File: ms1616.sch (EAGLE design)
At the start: 90 parts, among them IC101 ATMEGA32-PU, IC102 MAX483CPA, IC103 74594N, IC104 74594N, IC201 LTV847, IC202 LTV847, IC203 LTV847, IC204 LTV847, K301 S202S02, K302 S202S02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

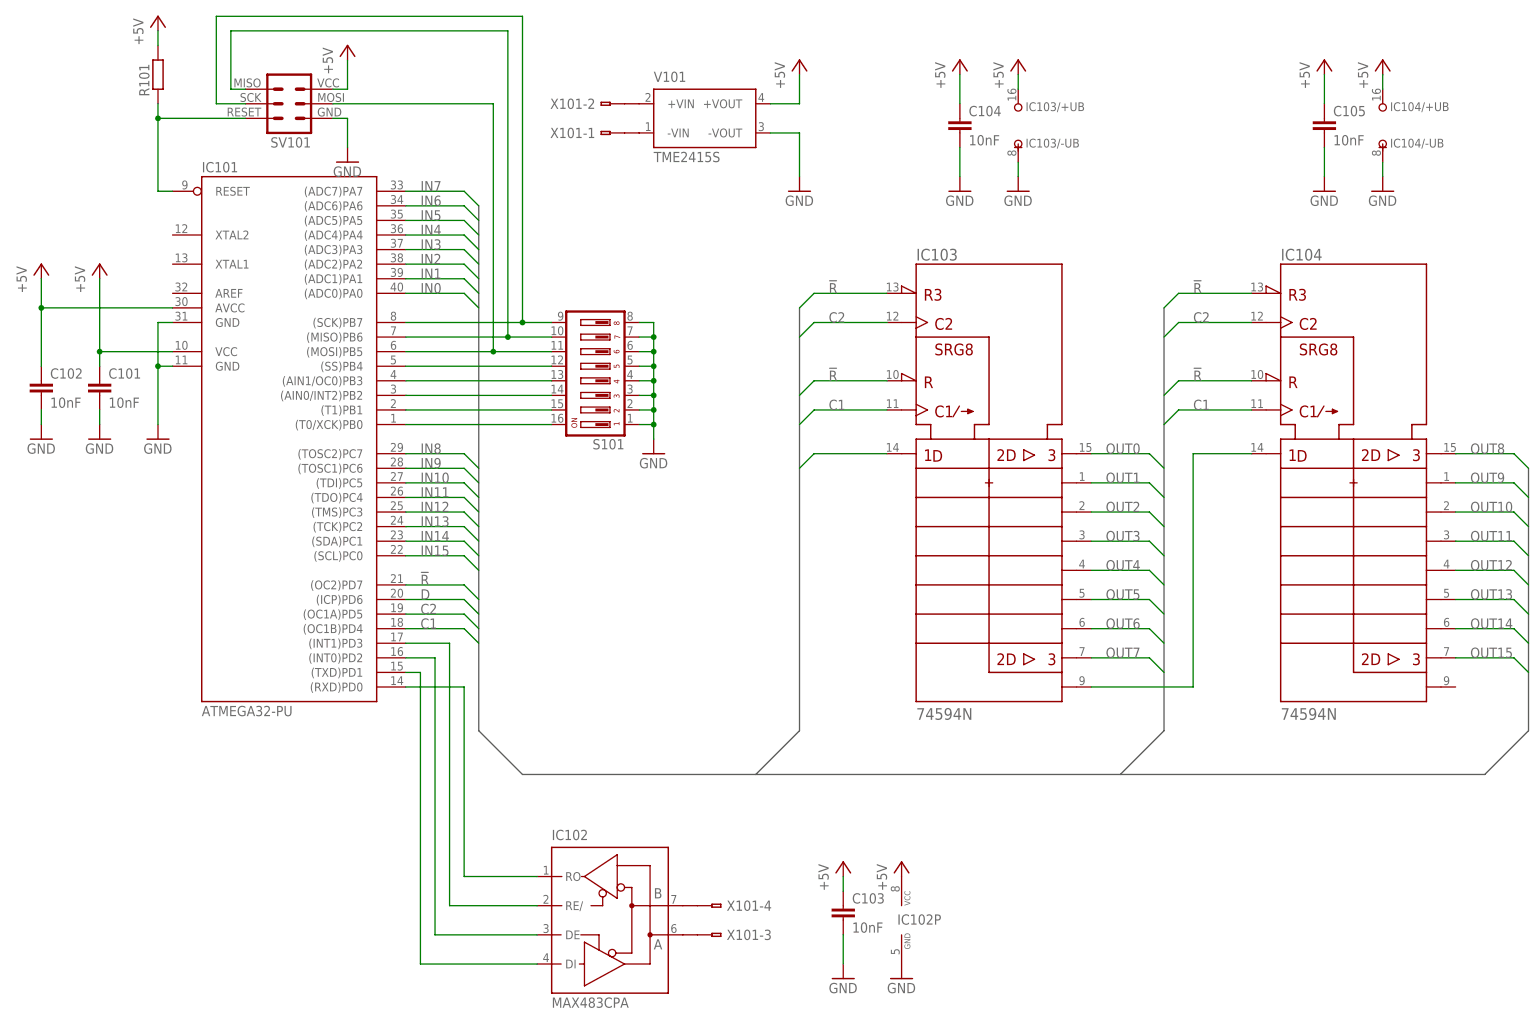
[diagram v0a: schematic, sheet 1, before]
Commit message: 74594 durch 74HC594 ersetzt
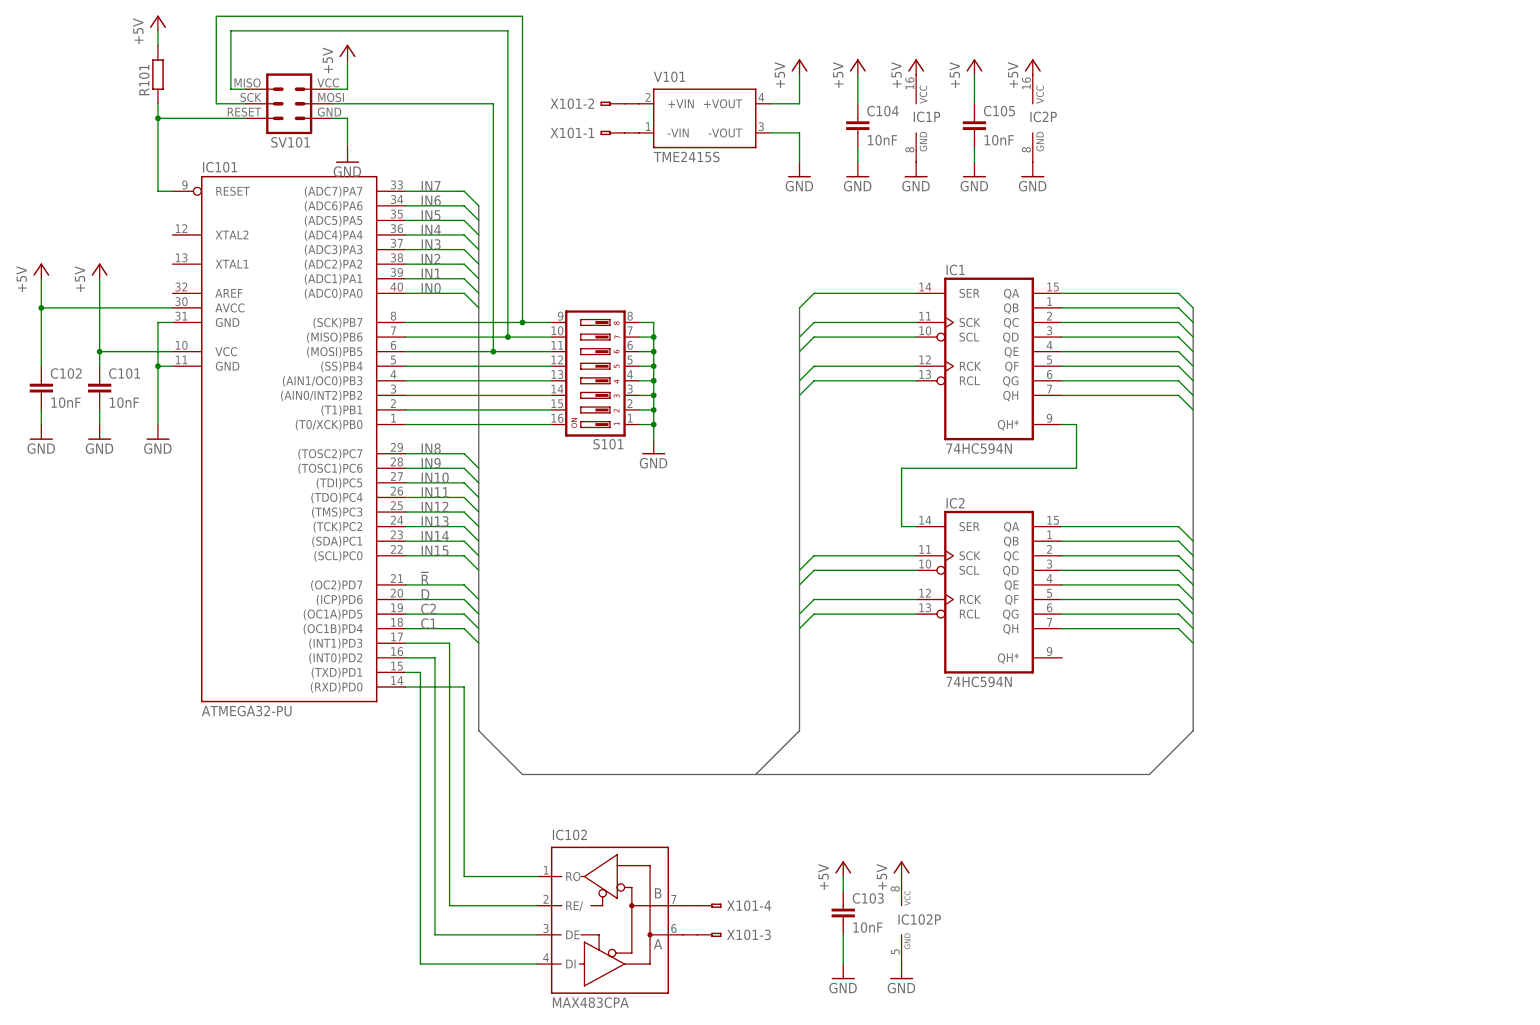
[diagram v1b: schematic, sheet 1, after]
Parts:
- removed IC103, IC104: 74594N, 74ttl-din:74594N
- added IC1, IC2: 74HC594N, 74xx-eu:74HC594N
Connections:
- net !R: now also IC1A.RCL, IC1A.SCL, IC2A.RCL, IC2A.SCL; no longer IC1031.!RCLR, IC1031.!SRCLR, IC1041.!RCLR, IC1041.!SRCLR
- net +5V: now also IC1P.VCC, IC2P.VCC; no longer IC103/+UB.+UB, IC104/+UB.+UB
- net C1: now also IC1A.SCK, IC2A.SCK; no longer IC1031.SRCK, IC1041.SRCK
- net C2: now also IC1A.RCK, IC2A.RCK; no longer IC1031.RCK, IC1041.RCK
- net D: now also IC1A.SER; no longer IC1031.SER
- net GND: now also IC1P.GND, IC2P.GND; no longer IC103/-UB.-UB, IC104/-UB.-UB
- net N$58: now also IC1A.QH*, IC2A.SER; no longer IC1031.QH*, IC1041.SER
- net OUT0: now also IC1A.QA; no longer IC1031.QA
- net OUT1: now also IC1A.QB; no longer IC1031.QB
- net OUT10: now also IC2A.QC; no longer IC1041.QC
- net OUT11: now also IC2A.QD; no longer IC1041.QD
- net OUT12: now also IC2A.QE; no longer IC1041.QE
- net OUT13: now also IC2A.QF; no longer IC1041.QF
- net OUT14: now also IC2A.QG; no longer IC1041.QG
- net OUT15: now also IC2A.QH; no longer IC1041.QH
- net OUT2: now also IC1A.QC; no longer IC1031.QC
- net OUT3: now also IC1A.QD; no longer IC1031.QD
- net OUT4: now also IC1A.QE; no longer IC1031.QE
- net OUT5: now also IC1A.QF; no longer IC1031.QF
- net OUT6: now also IC1A.QG; no longer IC1031.QG
- net OUT7: now also IC1A.QH; no longer IC1031.QH
- net OUT8: now also IC2A.QA; no longer IC1041.QA
- net OUT9: now also IC2A.QB; no longer IC1041.QB
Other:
- moved on the sheet: C104, C105

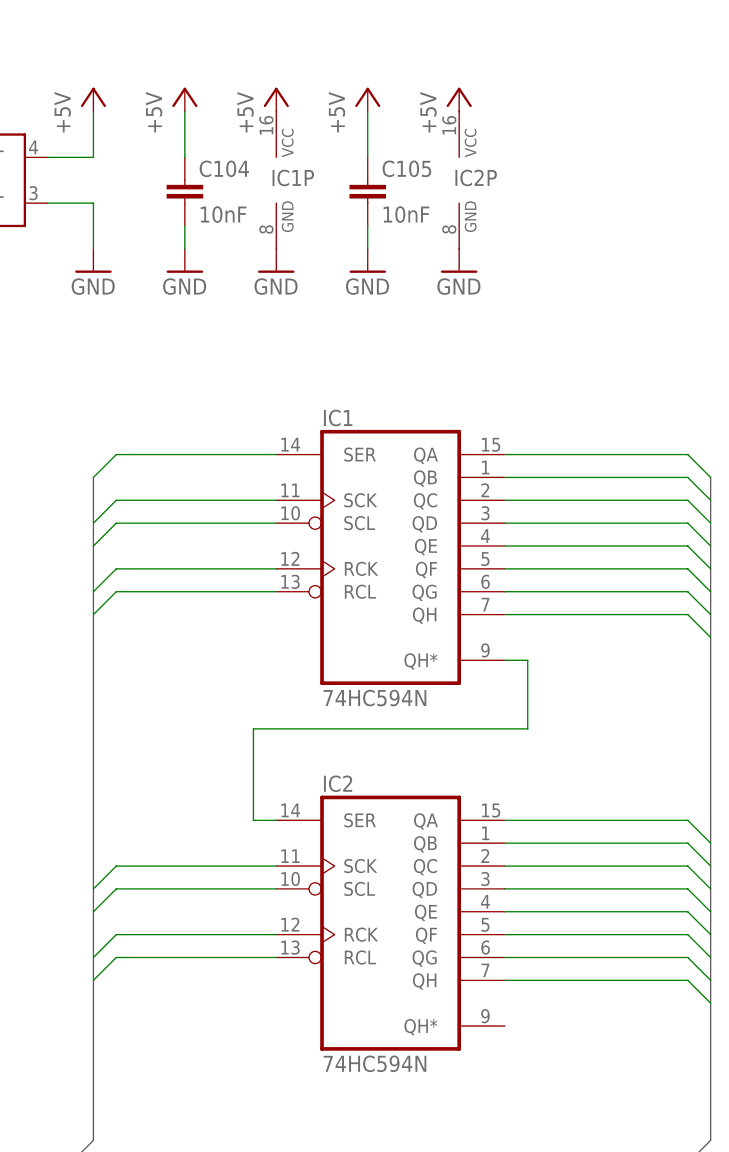
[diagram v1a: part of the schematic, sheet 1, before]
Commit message: Leichte korrekturen an Schematik und Layout
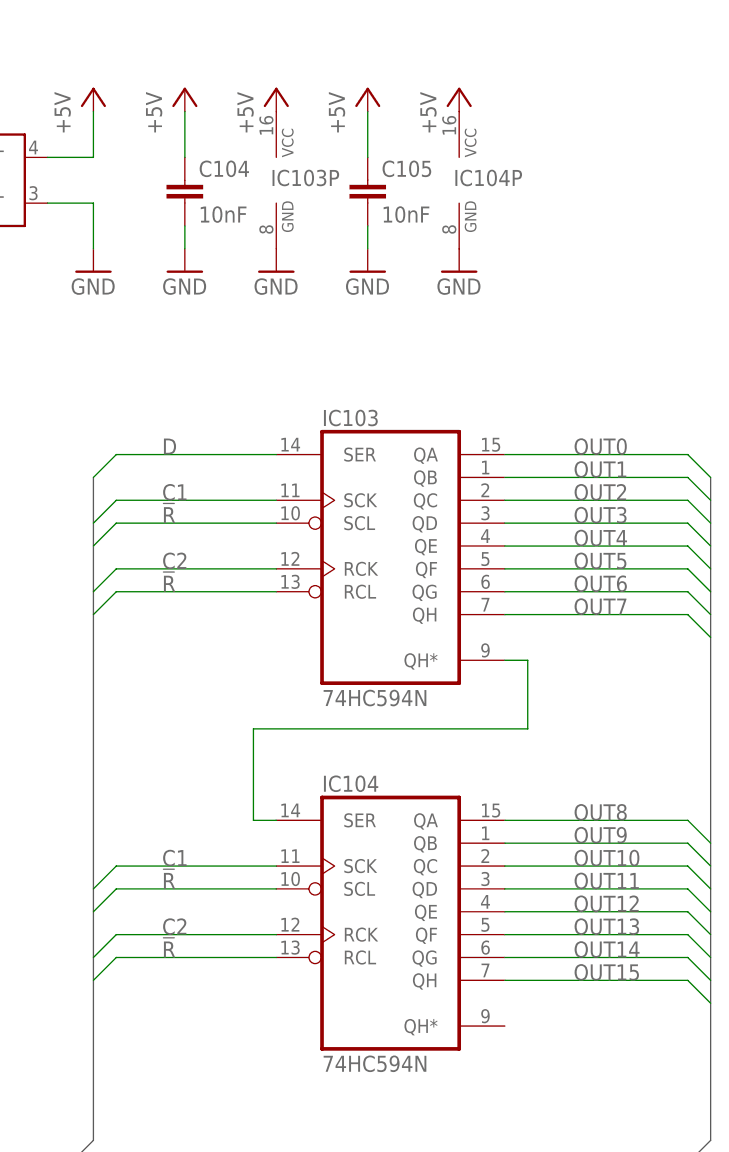
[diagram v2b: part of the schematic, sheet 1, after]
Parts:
- renumbered IC1 to IC103, IC2 to IC104

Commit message: Echtzeituhr eingebaut
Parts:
- added C1: 10nF, passiv:C_025-025X050
- added IC105: 74HC594N, 74xx-eu:74HC594N
- added Q1: (no value), passiv:Q_HC49S
- IC102: value MAX483CPA -> DS1337; device ic-wandler:MAX483CPA -> ic-controller:DS1337
- IC103: value 74HC594N -> MAX483CPA; device 74xx-eu:74HC594N -> ic-wandler:MAX483CPA
- S101: device schalter:DIP08YL -> schalter:DIP04YL
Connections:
- removed net N$128: IC101.(AIN0/INT2)PB2, S101.14
- removed net N$129: IC101.(AIN1/OC0)PB3, S101.13
- new net SCL: IC101.(T0/XCK)PB0, IC102G$1.SCL
- new net SDA: IC101.(T1)PB1, IC102G$1.SDA
- net !R: now also IC105A.RCL, IC105A.SCL; no longer IC103A.RCL, IC103A.SCL
- net +5V: now also C1.1, IC105P.VCC
- net C1: now also IC105A.SCK; no longer IC103A.SCK
- net C2: now also IC105A.RCK; no longer IC103A.RCK
- net D: now also IC104A.SER; no longer IC103A.SER
- net GND: now also C1.2, IC105P.GND; no longer S101.1, S101.2, S101.3, S101.4
- net N$122: now also S101.3; no longer S101.11
- net N$123: now also S101.2; no longer S101.10
- net N$124: now also IC103G$1.B; no longer IC102G$1.B
- net N$125: now also S101.1; no longer S101.9
- net N$126: now also IC102G$1.X1, Q1.2; no longer IC101.(T0/XCK)PB0, S101.16
- net N$127: now also IC102G$1.X2, Q1.1; no longer IC101.(T1)PB1, S101.15
- net N$130: now also S101.4; no longer S101.12
- net N$58: now also IC104A.QH*, IC105A.SER; no longer IC103A.QH*, IC104A.SER
- net N$61: now also IC103G$1.DI; no longer IC102G$1.DI
- net N$62: now also IC103G$1.RO; no longer IC102G$1.RO
- net N$63: now also IC103G$1.RE/; no longer IC102G$1.RE/
- net N$64: now also IC103G$1.DE; no longer IC102G$1.DE
- net N$74: now also IC103G$1.A; no longer IC102G$1.A
- net OUT0: now also IC104A.QA; no longer IC103A.QA
- net OUT1: now also IC104A.QB; no longer IC103A.QB
- net OUT10: now also IC105A.QC; no longer IC104A.QC
- net OUT11: now also IC105A.QD; no longer IC104A.QD
- net OUT12: now also IC105A.QE; no longer IC104A.QE
- net OUT13: now also IC105A.QF; no longer IC104A.QF
- net OUT14: now also IC105A.QG; no longer IC104A.QG
- net OUT15: now also IC105A.QH; no longer IC104A.QH
- net OUT2: now also IC104A.QC; no longer IC103A.QC
- net OUT3: now also IC104A.QD; no longer IC103A.QD
- net OUT4: now also IC104A.QE; no longer IC103A.QE
- net OUT5: now also IC104A.QF; no longer IC103A.QF
- net OUT6: now also IC104A.QG; no longer IC103A.QG
- net OUT7: now also IC104A.QH; no longer IC103A.QH
- net OUT8: now also IC105A.QA; no longer IC104A.QA
- net OUT9: now also IC105A.QB; no longer IC104A.QB
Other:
- moved on the sheet: IC102P, IC103P, IC104, IC104P, X101-3, X101-4

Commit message: Werte korrigiert
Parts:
- Q1: value (none) -> 32,768kHz
- R101: value (none) -> 10k
- V101: value TME2415S -> TME2405S; device schaltregler:TME2415S -> schaltregler:TME2405S; MPN (none) -> TME 2405S; OC_FARNELL (none) -> 1007547; OC_NEWARK (none) -> 51R5329
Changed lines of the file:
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@@
 <part name="GND25" library="versorgung" deviceset="GND" device=""/>
 <part name="P+2" library="versorgung" deviceset="+5V" device=""/>
-<part name="R101" library="passiv" deviceset="R_" device="0204/2V"/>
+<part name="R101" library="passiv" deviceset="R_" device="0204/2V" value="10k"/>
 <part name="P+1" library="versorgung" deviceset="+5V" device=""/>
 <part name="IC103" library="ic-wandler" deviceset="MAX48*" device="CPA" technology="3"/>
-<part name="V101" library="schaltregler" deviceset="TME?*" device="24" technology="15S"/>
+<part name="V101" library="schaltregler" deviceset="TME?*" device="24" technology="05S">
+<attribute name="MPN" value="TME 2405S"/>
+<attribute name="OC_FARNELL" value="1007547"/>
+<attribute name="OC_NEWARK" value="51R5329"/>
+</part>
 <part name="GND26" library="versorgung" deviceset="GND" device=""/>
 <part name="P+3" library="versorgung" deviceset="+5V" device=""/>
@@
 <part name="S101" library="schalter" deviceset="DIP04YL" device=""/>
 <part name="IC102" library="ic-controller" deviceset="DS1337" device=""/>
-<part name="Q1" library="passiv" deviceset="Q_" device="HC49S"/>
+<part name="Q1" library="passiv" deviceset="Q_" device="HC49S" value="32,768kHz"/>
 <part name="C1" library="passiv" deviceset="C_" device="025-025X050" value="10nF"/>
 <part name="P+12" library="versorgung" deviceset="+5V" device=""/>
@@
 <instance part="GND42" gate="1" x="182.88" y="5.08"/>
 <instance part="GND43" gate="1" x="172.72" y="5.08"/>
-<instance part="GND44" gate="1" x="139.7" y="96.52"/>
+<instance part="GND44" gate="1" x="139.7" y="106.68"/>
 <instance part="IC104" gate="A" x="198.12" y="114.3"/>
 <instance part="IC104" gate="P" x="185.42" y="154.94"/>
@@
 <segment>
 <pinref part="GND44" gate="1" pin="GND"/>
-<wire x1="137.16" y1="101.6" x2="139.7" y2="101.6" width="0.1524" layer="91"/>
-<wire x1="139.7" y1="101.6" x2="139.7" y2="99.06" width="0.1524" layer="91"/>
-<wire x1="137.16" y1="104.14" x2="139.7" y2="104.14" width="0.1524" layer="91"/>
-<wire x1="139.7" y1="104.14" x2="139.7" y2="101.6" width="0.1524" layer="91"/>
-<junction x="139.7" y="101.6"/>
-<wire x1="137.16" y1="106.68" x2="139.7" y2="106.68" width="0.1524" layer="91"/>
-<wire x1="139.7" y1="106.68" x2="139.7" y2="104.14" width="0.1524" layer="91"/>
-<junction x="139.7" y="104.14"/>
-<wire x1="137.16" y1="109.22" x2="139.7" y2="109.22" width="0.1524" layer="91"/>
-<wire x1="139.7" y1="109.22" x2="139.7" y2="106.68" width="0.1524" layer="91"/>
-<junction x="139.7" y="106.68"/>
 <wire x1="137.16" y1="111.76" x2="139.7" y2="111.76" width="0.1524" layer="91"/>
 <wire x1="139.7" y1="111.76" x2="139.7" y2="109.22" width="0.1524" layer="91"/>
-<junction x="139.7" y="109.22"/>
 <wire x1="137.16" y1="114.3" x2="139.7" y2="114.3" width="0.1524" layer="91"/>
 <wire x1="139.7" y1="114.3" x2="139.7" y2="111.76" width="0.1524" layer="91"/>
@@
 <segment>
 <pinref part="SV101" gate="1" pin="MISO"/>
-<wire x1="68.58" y1="160.02" x2="66.04" y2="160.02" width="0.1524" layer="91"/>
-<wire x1="66.04" y1="160.02" x2="66.04" y2="170.18" width="0.1524" layer="91"/>
-<wire x1="66.04" y1="170.18" x2="114.3" y2="170.18" width="0.1524" layer="91"/>
+<wire x1="68.58" y1="160.02" x2="63.5" y2="160.02" width="0.1524" layer="91"/>
+<wire x1="63.5" y1="160.02" x2="63.5" y2="170.18" width="0.1524" layer="91"/>
+<wire x1="63.5" y1="170.18" x2="114.3" y2="170.18" width="0.1524" layer="91"/>
 <wire x1="114.3" y1="170.18" x2="114.3" y2="116.84" width="0.1524" layer="91"/>
 <pinref part="IC101" gate="G$1" pin="(MISO)PB6"/>
@@
 <segment>
 <pinref part="SV101" gate="1" pin="SCK"/>
-<wire x1="68.58" y1="157.48" x2="63.5" y2="157.48" width="0.1524" layer="91"/>
-<wire x1="63.5" y1="157.48" x2="63.5" y2="172.72" width="0.1524" layer="91"/>
-<wire x1="63.5" y1="172.72" x2="116.84" y2="172.72" width="0.1524" layer="91"/>
+<wire x1="68.58" y1="157.48" x2="60.96" y2="157.48" width="0.1524" layer="91"/>
+<wire x1="60.96" y1="157.48" x2="60.96" y2="172.72" width="0.1524" layer="91"/>
+<wire x1="60.96" y1="172.72" x2="116.84" y2="172.72" width="0.1524" layer="91"/>
 <wire x1="116.84" y1="172.72" x2="116.84" y2="119.38" width="0.1524" layer="91"/>
 <pinref part="IC101" gate="G$1" pin="(SCK)PB7"/>
@@
 <wire x1="152.4" y1="83.82" x2="162.56" y2="83.82" width="0.1524" layer="91"/>
 <wire x1="162.56" y1="83.82" x2="165.1" y2="81.28" width="0.1524" layer="91"/>
+<label x="154.94" y="83.82" size="1.778" layer="95"/>
 </segment>
 </net>
@@
 <wire x1="152.4" y1="81.28" x2="162.56" y2="81.28" width="0.1524" layer="91"/>
 <wire x1="162.56" y1="81.28" x2="165.1" y2="78.74" width="0.1524" layer="91"/>
-</segment>
-</net>
+<label x="154.94" y="81.28" size="1.778" layer="95"/>
+</segment>
+</net>
